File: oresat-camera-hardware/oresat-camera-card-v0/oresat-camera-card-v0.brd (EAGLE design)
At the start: 99.8 x 94.7 mm, 320 parts, among them J1 J-SAMTEC-TFM-120-X1-XXX-D-RA, J2 DM3BT-DSF-PEJS, J4 3-1734592-64-1734592-0, J8 2-1734592-0, Q1 DMP2240UDM, Q3 MIC842, Q4 MIC842, Q5 PMV45EN, Q6 MOSFET-PCH-SOT23-6, Q7 MOSFET-PCH-SOT23-6, Q8 PMV45EN, Q9 MMBT2907, U1 MAX7310ATE, U10 SN74LVC8T245MPWREPPW24-M, U11 RCLAMP0504FB, U12 RCLAMP0504FB, U13 TPS2051CDBVR, U14 TLVH431, U15 SN74LVC1G07DCK, U2 TPS62112, U3 MAX4211CETE, U4 TCAN330, U5 CLVCH16T245MDGGREP, U6 OSD3358-512M-BSM, U7 TCA9509DGKRDGK8-M, U9 TLV70028QDDCRQ1, Y1 24MHz

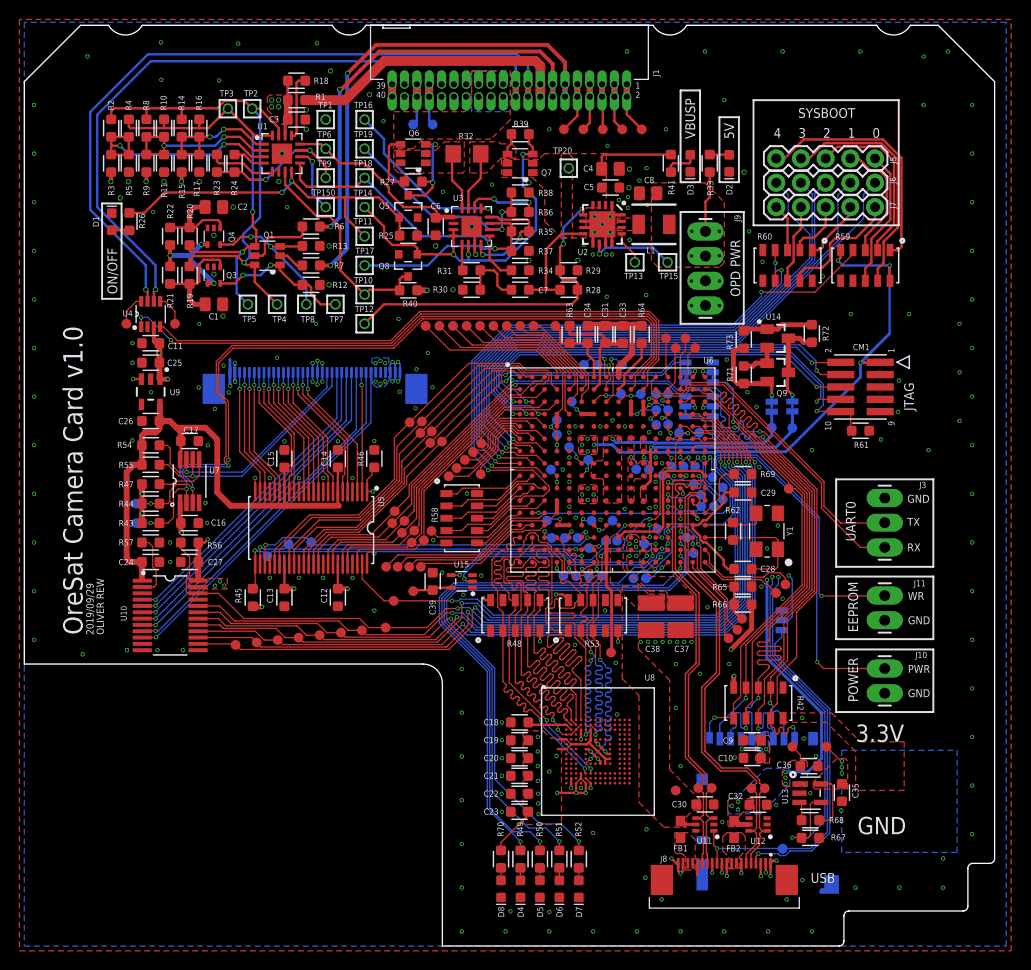
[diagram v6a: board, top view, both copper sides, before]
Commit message: added VDD caps
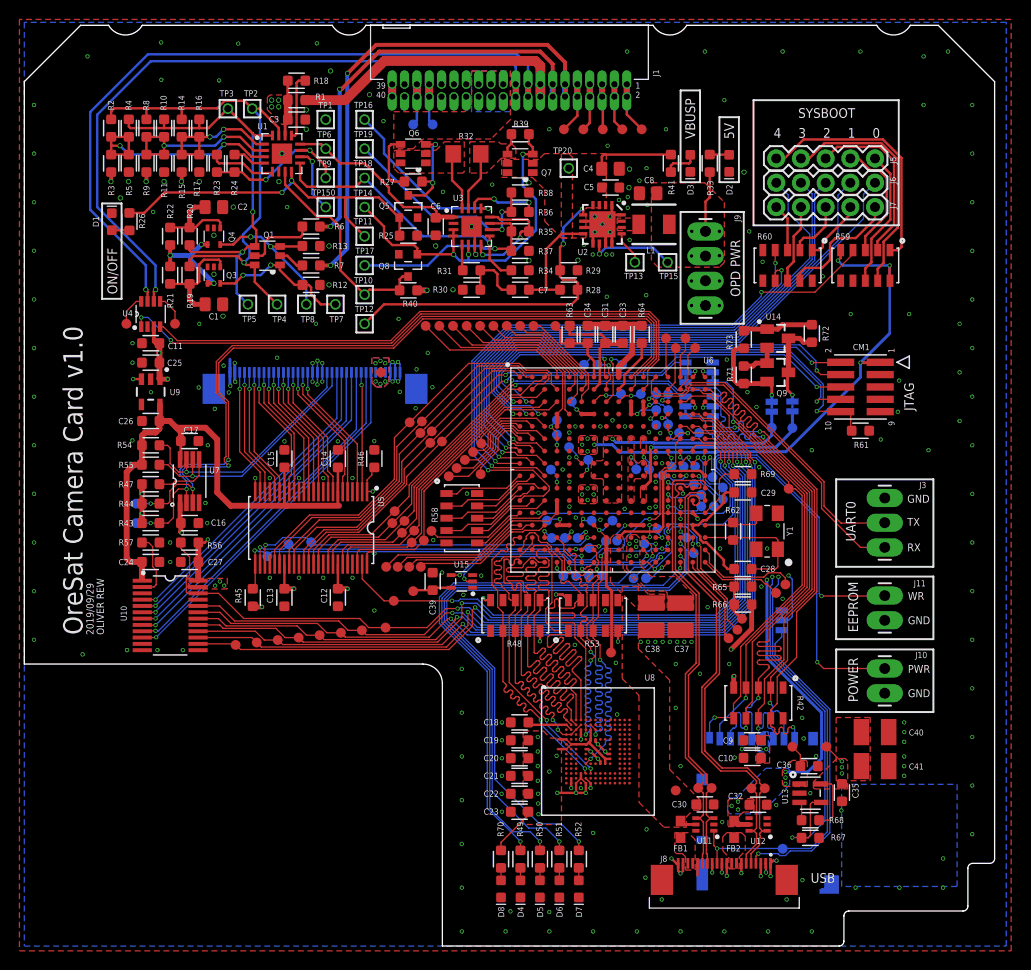
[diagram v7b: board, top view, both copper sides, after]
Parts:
- added C40, C41: 22uF, oresat-rcl:C1210
- added TP152: TEST-POINT3X4, SparkFun-Connectors:PAD.03X.04
- moved U$2 3.50 mm to (90.0, 11.5)
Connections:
- removed net N$403: TP118.P$1, U6.N7
- net 3.3V: now also TP152.P$1
- net GND: now also C40.2, C41.2
- net N$401: now also TP118.P$1, U6.N7
- net VDD: now also C40.1, C41.1
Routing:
- net N$401: track 12.1 -> 15.7 mm, vias 0 -> 1
- net N$403: track 2.51 -> 0.00 mm, vias 1 -> 0
- net GND: vias 269 -> 275
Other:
- board text removed: "3.3V"
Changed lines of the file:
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@@
 <setting verticaltext="up"/>
 </settings>
-<grid distance="1.5" unitdist="mm" unit="mm" style="lines" multiple="1" display="yes" altdistance="0.0625" altunitdist="mm" altunit="mm"/>
+<grid distance="0.5" unitdist="mm" unit="mm" style="lines" multiple="1" display="yes" altdistance="0.0625" altunitdist="mm" altunit="mm"/>
 <layers>
 <layer number="1" name="Top" color="4" fill="1" visible="yes" active="yes"/>
@@
 Thermals on SIP power planes?</text>
 <wire x1="42.53125" y1="50.96875" x2="38.53125" y2="54.96875" width="0" layer="48"/>
-<polygon width="0.127" layer="29">
-<vertex x="86" y="20.5"/>
-<vertex x="90" y="20.5"/>
-<vertex x="90" y="16.5"/>
-<vertex x="86" y="16.5"/>
-</polygon>
-<text x="85.5" y="21" size="1.778" layer="21" font="vector" ratio="20">3.3V</text>
-<polygon width="0.127" layer="29">
-<vertex x="86" y="11"/>
-<vertex x="90" y="11"/>
-<vertex x="90" y="7"/>
-<vertex x="86" y="7"/>
-</polygon>
-<text x="85.6875" y="11.5" size="1.778" layer="21" font="vector" ratio="20">GND</text>
 <text x="-54.5" y="47" size="1.778" layer="48" font="vector" ratio="0">TODO
 Smaller headers?
@@
 </element>
 <element name="TP151" library="SparkFun-Connectors" package="PAD.03X.04" value="TEST-POINT3X4" x="56.3125" y="56" smashed="yes" rot="MR0"/>
-<element name="U$2" library="psas-logo" package="PSAS_LOGO_10X10" value="" x="90" y="15" smashed="yes" rot="MR0"/>
+<element name="U$2" library="psas-logo" package="PSAS_LOGO_10X10" value="" x="90" y="11.5" smashed="yes" rot="MR0"/>
+<element name="TP152" library="SparkFun-Connectors" package="PAD.03X.04" value="TEST-POINT3X4" x="36.6875" y="59" smashed="yes"/>
+<element name="C40" library="oresat-rcl" package="C1210" value="22uF" x="87.5" y="22" smashed="yes">
+<attribute name="NAME" x="90.978" y="21.651" size="0.625" layer="25" ratio="20"/>
+<attribute name="VALUE" x="86.103" y="19.079" size="1.27" layer="27"/>
+</element>
+<element name="C41" library="oresat-rcl" package="C1210" value="22uF" x="87.5" y="18.5" smashed="yes">
+<attribute name="NAME" x="90.978" y="18.151" size="0.625" layer="25" ratio="20"/>
+<attribute name="VALUE" x="86.103" y="15.579" size="1.27" layer="27"/>
+</element>
 </elements>
 <signals>
@@
 <wire x1="74.80625" y1="32.61875" x2="72.6875" y2="30.5" width="0.508" layer="1"/>
 <via x="72.6875" y="30.5" extent="1-16" drill="0.254"/>
-<polygon width="0.127" layer="1">
-<vertex x="77.78125" y="23.96875"/>
-<vertex x="83.01814375" y="23.97404375"/>
-<vertex x="86" y="21"/>
-<vertex x="90.5" y="21"/>
-<vertex x="90.5" y="16"/>
-<vertex x="85.5" y="16"/>
-<vertex x="85.5" y="20"/>
-<vertex x="82.5" y="23"/>
-<vertex x="77.78125" y="23"/>
-</polygon>
 <wire x1="52.875" y1="13.5625" x2="52.875" y2="21.4375" width="2.54" layer="15"/>
 <wire x1="52.875" y1="21.4375" x2="52.8125" y2="21.5" width="2.54" layer="15"/>
@@
 <wire x1="89" y1="68.4652" x2="89" y2="70" width="0.254" layer="1"/>
 <wire x1="89" y1="63" x2="89" y2="70" width="0.254" layer="16"/>
+<contactref element="TP152" pad="P$1"/>
+<polygon width="0.15" layer="1" thermals="no">
+<vertex x="35.75" y="60.5"/>
+<vertex x="35.75" y="57.9375"/>
+<vertex x="36.1875" y="57.5"/>
+<vertex x="37" y="57.5"/>
+<vertex x="37.5" y="58"/>
+<vertex x="37.5" y="60.5"/>
+</polygon>
+<wire x1="80" y1="23.46875" x2="78.04" y2="23.4252" width="0" layer="19" extent="1-1"/>
 </signal>
 <signal name="SDAOPT2">
@@
 <via x="72" y="87" extent="1-16" drill="0.254"/>
 <polygon width="0.127" layer="16" orphans="yes">
-<vertex x="84.0625" y="20.125"/>
-<vertex x="95.9375" y="20.125"/>
-<vertex x="95.9375" y="9.625"/>
-<vertex x="84.0625" y="9.625"/>
+<vertex x="84.0625" y="16.625"/>
+<vertex x="95.9375" y="16.625"/>
+<vertex x="95.9375" y="6.125"/>
+<vertex x="84.0625" y="6.125"/>
 </polygon>
 <via x="31.5" y="90" extent="1-16" drill="0.35"/>
 <via x="35.5" y="87.5625" extent="1-16" drill="0.35"/>
+<contactref element="C40" pad="2"/>
+<contactref element="C41" pad="2"/>
+<via x="90.5" y="23" extent="1-16" drill="0.254"/>
+<via x="90.5" y="22" extent="1-16" drill="0.254"/>
+<via x="90.5" y="21" extent="1-16" drill="0.254"/>
+<via x="90.5" y="19.5" extent="1-16" drill="0.254"/>
+<via x="90.5" y="18.5" extent="1-16" drill="0.254"/>
+<via x="90.5" y="17.5" extent="1-16" drill="0.254"/>
 <wire x1="92.5" y1="91.5" x2="95" y2="92" width="0" layer="19" extent="1-1"/>
 <wire x1="92.5" y1="86.5" x2="92.5" y2="91.5" width="0" layer="19" extent="1-1"/>
@@
 <wire x1="74.5625" y1="73.5" x2="75.96" y2="71.5748" width="0" layer="19" extent="1-1"/>
 <wire x1="88.5" y1="46.08" x2="88.09375" y2="52.09375" width="0" layer="19" extent="1-1"/>
+<wire x1="88.9" y1="18.5" x2="84.09375" y2="14.88125" width="0" layer="19" extent="1-1"/>
+<wire x1="90.5" y1="18.5" x2="88.9" y2="18.5" width="0" layer="19" extent="1-1"/>
+<wire x1="90.5" y1="19.5" x2="90.5" y2="18.5" width="0" layer="19" extent="1-1"/>
+<wire x1="90.5" y1="17.5" x2="90.5" y2="18.5" width="0" layer="19" extent="1-1"/>
+<wire x1="90.5" y1="21" x2="90.5" y2="19.5" width="0" layer="19" extent="1-1"/>
+<wire x1="90.5" y1="22" x2="90.5" y2="21" width="0" layer="19" extent="1-1"/>
+<wire x1="90.5" y1="23" x2="90.5" y2="22" width="0" layer="19" extent="1-1"/>
+<wire x1="88.9" y1="22" x2="90.5" y2="22" width="0" layer="19" extent="1-1"/>
+<wire x1="88.5" y1="26" x2="90.5" y2="23" width="0" layer="19" extent="1-1"/>
 <wire x1="74.03125" y1="79.59375" x2="74.5625" y2="73.5" width="0" layer="19" extent="1-1"/>
 <wire x1="72.5" y1="79.623" x2="74.03125" y2="79.59375" width="0" layer="19" extent="1-1"/>
@@
 <wire x1="45.53125" y1="46.53125" x2="43.4252" y2="41.46" width="0" layer="19" extent="1-1"/>
 <wire x1="46.5748" y1="46.54" x2="45.53125" y2="46.53125" width="0" layer="19" extent="1-1"/>
+<wire x1="88.5" y1="33.5" x2="88.5" y2="26" width="0" layer="19" extent="1-1"/>
 <wire x1="64.945" y1="44.555" x2="71.5625" y2="40.875" width="0" layer="19" extent="1-1"/>
 <wire x1="64.9375" y1="45.1875" x2="64.945" y2="44.555" width="0" layer="19" extent="1-1"/>
@@
 <wire x1="20.03125" y1="89.03125" x2="14.09375" y2="89.09375" width="0" layer="19" extent="1-1"/>
 <wire x1="22" y1="92.8125" x2="20.03125" y2="89.03125" width="0" layer="19" extent="1-1"/>
-<wire x1="88.5" y1="26" x2="81.13125" y2="21.325" width="0" layer="19" extent="16-16"/>
-<wire x1="88.5" y1="33.5" x2="88.5" y2="26" width="0" layer="19" extent="1-1"/>
 </signal>
 <signal name="N$262">
@@
 <wire x1="60.405" y1="30.2439" x2="60.34375" y2="30.1875" width="0.127" layer="1"/>
 <wire x1="60.405" y1="36.50235" x2="60.405" y2="30.2439" width="0.3048" layer="1"/>
-</signal>
-<signal name="N$403">
 <contactref element="TP118" pad="P$1"/>
 <contactref element="U6" pad="N7"/>
@@
 <wire x1="60.5" y1="43.75" x2="59.53125" y2="42.78125" width="0.127" layer="16"/>
 <wire x1="59.53125" y1="42.78125" x2="59.125" y2="42.78125" width="0.127" layer="16"/>
+<wire x1="59.125" y1="42.78125" x2="59.865" y2="42.04125" width="0.127" layer="1"/>
+<wire x1="59.865" y1="42.04125" x2="59.865" y2="42.015" width="0.127" layer="1"/>
 </signal>
 <signal name="N$404">
@@
 <wire x1="79.81875" y1="18.5" x2="79.81875" y2="19.68125" width="0.127" layer="1"/>
 <wire x1="79.81875" y1="19.68125" x2="79" y2="20.5" width="0.127" layer="1"/>
-<wire x1="78.28125" y1="17.90625" x2="79.81875" y2="18.5" width="0" layer="19" extent="1-1"/>
-<wire x1="78.28125" y1="17.3125" x2="78.28125" y2="17.90625" width="0" layer="19" extent="1-1"/>
-<wire x1="78.28125" y1="16.6875" x2="78.28125" y2="17.3125" width="0" layer="19" extent="1-1"/>
-<wire x1="79.72615" y1="16.66875" x2="78.28125" y2="16.6875" width="0" layer="19" extent="1-1"/>
-<wire x1="74.56875" y1="14.53125" x2="78.28125" y2="16.6875" width="0" layer="19" extent="1-1"/>
-<wire x1="73.40625" y1="14.84375" x2="74.56875" y2="14.53125" width="0" layer="19" extent="1-1"/>
-<wire x1="72.75" y1="14.40625" x2="73.40625" y2="14.84375" width="0" layer="19" extent="1-1"/>
-<wire x1="73.40625" y1="14.03125" x2="72.75" y2="14.40625" width="0" layer="19" extent="1-1"/>
-<wire x1="73" y1="12.85" x2="73.40625" y2="14.03125" width="0" layer="19" extent="1-1"/>
 </signal>
 <signal name="AGND">
@@
 <wire x1="83.15625" y1="16.5" x2="83.15625" y2="13.3125" width="0.127" layer="1"/>
 <wire x1="83.15625" y1="13.3125" x2="82.78125" y2="12.9375" width="0.127" layer="1"/>
+<contactref element="C40" pad="1"/>
+<contactref element="C41" pad="1"/>
+<polygon width="0.127" layer="1" thermals="no">
+<vertex x="84" y="17"/>
+<vertex x="87" y="17"/>
+<vertex x="87" y="23.5"/>
+<vertex x="83.5" y="23.5"/>
+<vertex x="83.5" y="17"/>
+</polygon>
 <wire x1="58.595" y1="45.825" x2="58.5625" y2="46.4375" width="0" layer="19" extent="1-1"/>
 <wire x1="58.595" y1="47.095" x2="58.5625" y2="46.4375" width="0" layer="19" extent="1-1"/>
@@
 <wire x1="84.09375" y1="17.75" x2="84.09375" y2="18.375" width="0" layer="19" extent="1-1"/>
 <wire x1="84.09375" y1="16.68125" x2="84.09375" y2="17.75" width="0" layer="19" extent="1-1"/>
+<wire x1="86.1" y1="18.5" x2="84.09375" y2="18.375" width="0" layer="19" extent="1-1"/>
 <wire x1="81.96135" y1="16.66875" x2="84.09375" y2="16.68125" width="0" layer="19" extent="1-1"/>
+<wire x1="86.1" y1="22" x2="86.1" y2="18.5" width="0" layer="19" extent="1-1"/>
 </signal>
 <signal name="N$82">

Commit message: added holes for lens mount
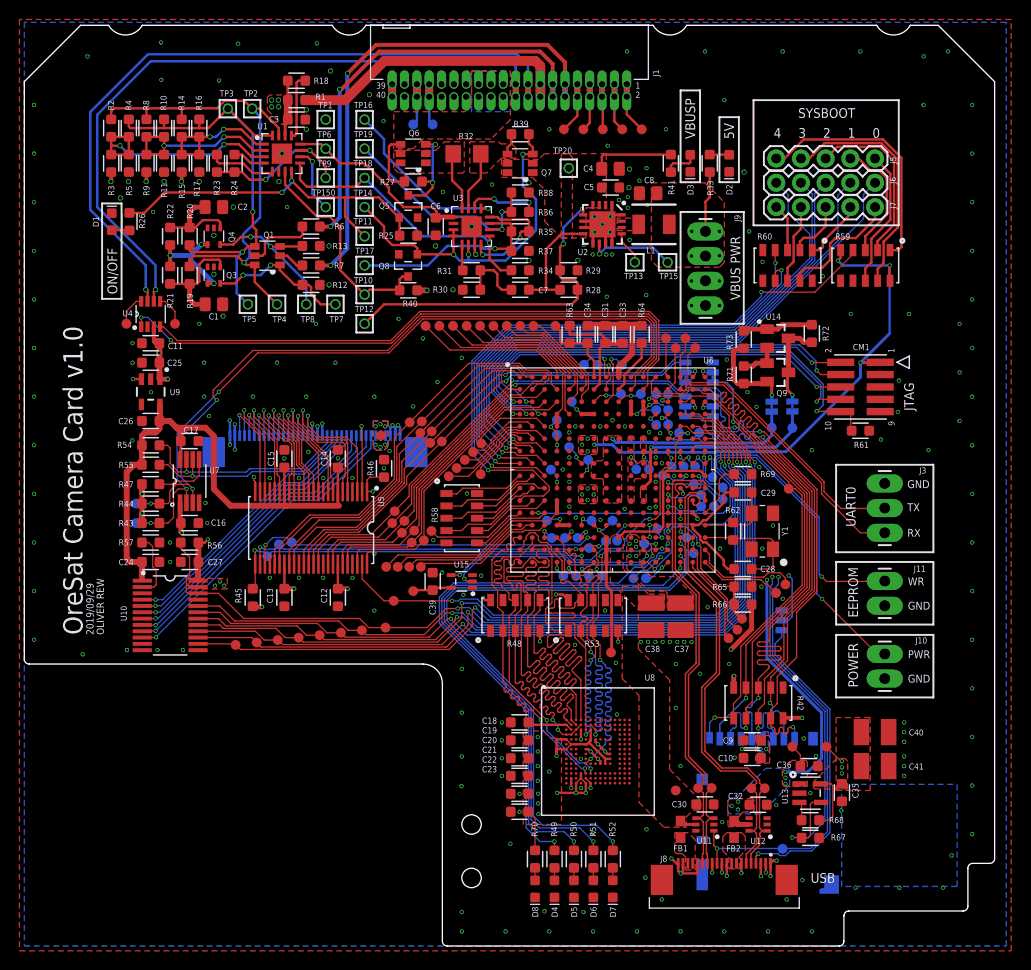
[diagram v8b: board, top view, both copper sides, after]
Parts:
- moved J4 6.50 mm to (29.9, 52.5)
- moved TP152 6.50 mm to (36.7, 52.5)
- moved D4 3.50 mm to (54.5, 5.88)
- moved D5 3.50 mm to (56.5, 5.88)
- moved D6 3.50 mm to (58.5, 5.88)
- moved D7 3.50 mm to (60.5, 5.88)
- moved D8 3.50 mm to (52.5, 5.88)
- moved R49 3.50 mm to (54.5, 8.94)
- moved R50 3.50 mm to (56.5, 8.94)
- moved R51 3.50 mm to (58.5, 8.94)
- moved R52 3.50 mm to (60.5, 8.94)
- moved R70 3.50 mm to (52.5, 8.94)
- moved TP44 2.00 mm to (27.5, 41.5)
- moved J10 1.50 mm to (88.5, 27.5)
- moved J11 1.50 mm to (88.5, 35.0)
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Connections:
- net GND: now also U8.J5
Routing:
- net 3.3V: track 202.2 -> 210.6 mm
- net SADDR_E: track 36.2 -> 31.0 mm
- net STANDBY_E: track 34.2 -> 29.0 mm
- net !RESET_E: track 33.3 -> 28.2 mm
- net CLK_EN_E: track 32.5 -> 27.4 mm
- net TRIGGER_E: track 37.1 -> 32.0 mm
- net GND: track 58.5 -> 53.4 mm
- net VREG_EN_E: track 37.8 -> 32.9 mm
- net !OE_E: track 35.0 -> 30.2 mm
- net SDA_2: track 82.6 -> 77.8 mm
- net N$525: track 55.6 -> 50.9 mm
- net SCL_2: track 80.5 -> 75.8 mm
- net FLASH_E: track 12.3 -> 7.76 mm
- net N$656: track 62.4 -> 65.8 mm
- net I2C2_SCL: track 25.8 -> 22.6 mm
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- added copper zone on layer 15, net GND
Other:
- outline, holes or cut-outs redrawn
- board text added: "Camera Lens Center Line"
- board text added: "FFC Cable Center Line"
- board text added: "Min. Cable Length: 28.625mm FFC Cable: Molex 0151660381 29.97mm"
- board text added: "TODO Smaller headers?"
- board text added: "VBUS PWR"
- board text removed: "OPD PWR"
- board text removed: "TODO Smaller headers? PSAS LOGO?"
- board text removed: "TODO Thermals on SIP power planes?"
